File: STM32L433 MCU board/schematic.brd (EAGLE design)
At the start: 55 x 60 mm, 15 parts, among them T1 2N2222, U1 STM32L433CCT6, Y1 ECS-160-8-30B-CKM

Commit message: Add files via upload
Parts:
- removed R1: 1k, SparkFun-Resistors:0603
- removed R2: 220, SparkFun-Resistors:0603
- removed R3: 44.2k, SparkFun-Resistors:0603
- removed R4: 16k, SparkFun-Resistors:0603
- removed R5, R6: 10k, SparkFun-Resistors:0603
- removed Y1: ECS-160-8-30B-CKM, ECS-160-8-30B-CKM:XTAL_ECS-160-8-30B-CKM
- added R10: 1k, adafruit:R0805
- added R11, R12: 10k, adafruit:R0805
- added R7: 44.2k, adafruit:R0805
- added R8: 16k, adafruit:R0805
- added R9: 220, adafruit:R0805
- moved LS1 62.0 mm to (34.3, 47.0)
- moved JP4 2.54 mm to (21.6, 26.7)
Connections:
- removed net N$7: Y1.2, Y1.4
- new net SD_CS: U$1.2, U1.40
- net 3.3V: now also R11.1, R12.1; no longer R5.2, R6.2
- net BUZZ: now also R9.1, U1.29; no longer R2.1
- net CS1: now also U1.41
- net CS2: now also U1.42
- net CS3: now also U1.43
- net CS4: now also U1.45
- net CS5: now also U1.46
- net GND: now also R8.1; no longer R4.1
- net IGN_CHK1: now also U1.11, U1.12
- net IGN_CHK2: now also U1.13
- net IGN_CHK3: now also U1.14
- net LIPO: now also R10.2, R7.2; no longer R1.2, R3.2
- net N$2: now also R9.2; no longer R2.2
- net N$3: now also R10.1; no longer R1.1
- net N$4: now also R11.2; no longer R6.1
- net N$5: now also R7.1, R8.2, U1.10; no longer R3.1, R4.2
- net N$6: now also R12.2; no longer R5.1

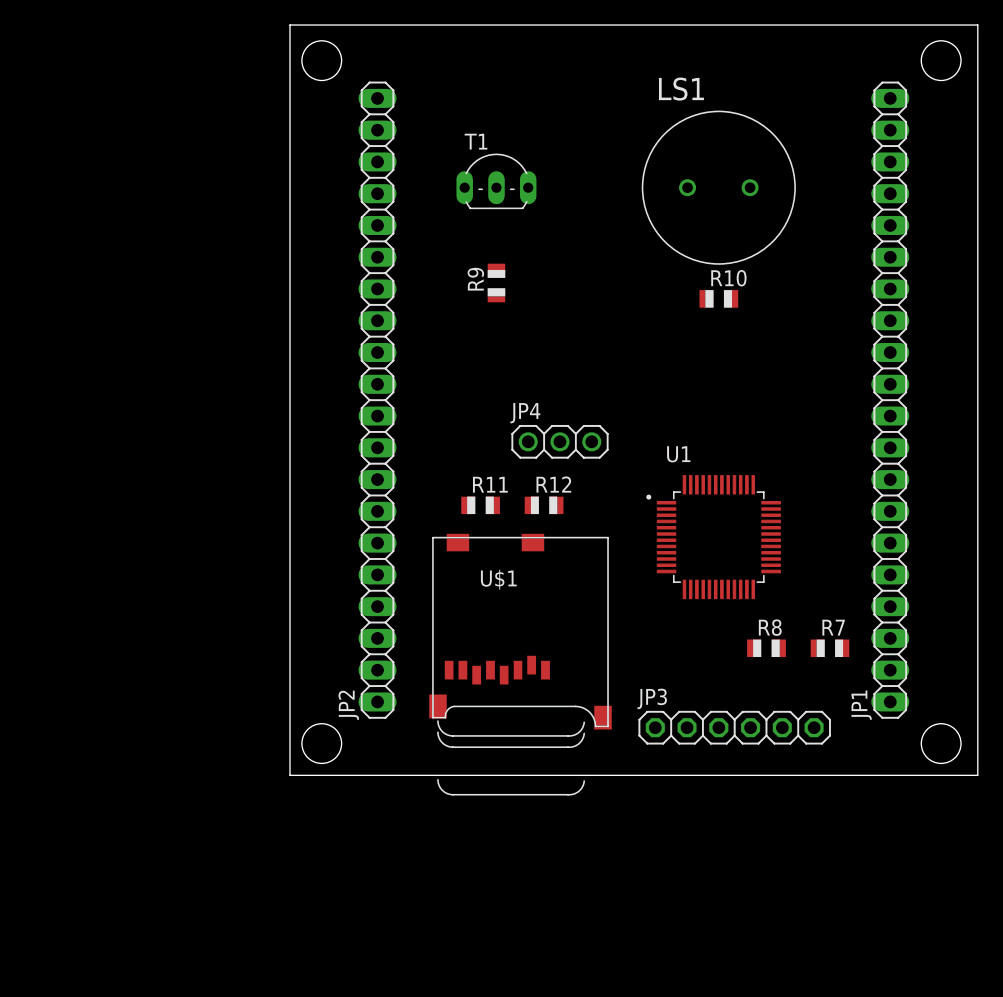
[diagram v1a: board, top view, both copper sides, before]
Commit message: Finished MCU board routing
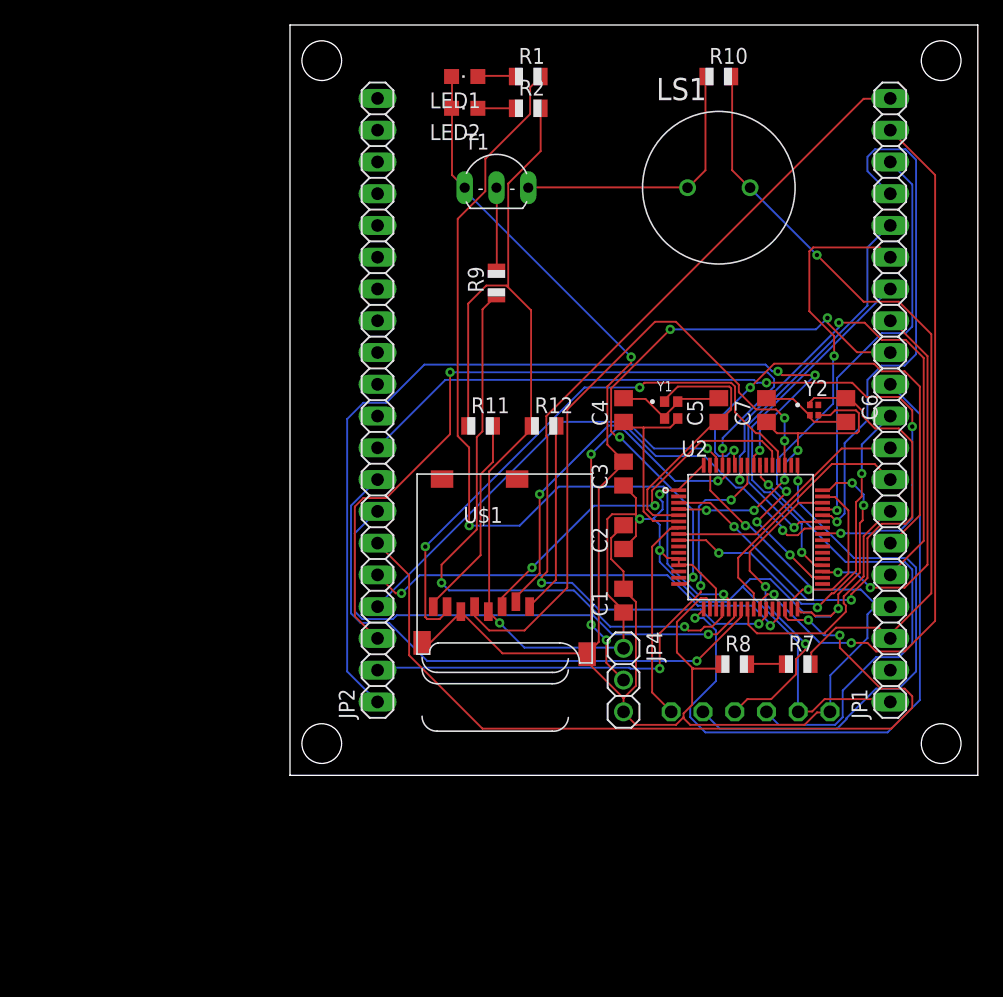
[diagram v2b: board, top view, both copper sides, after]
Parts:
- removed U1: STM32L433CCT6, STM32L433CCT6:QFP50P900X900X160-48N
- added C1: 10nF, rcl:C0805
- added C2: 0.1uF, rcl:C0805
- added C3: 1uF, rcl:C0805
- added C4, C5: 8pF, rcl:C0805
- added C6, C7: 6pF, rcl:C0805
- added LED1: RED, adafruit:CHIPLED_0805
- added LED2: GREEN, adafruit:CHIPLED_0805
- added R1: 130, adafruit:R0805
- added R2: 110, adafruit:R0805
- added U2: STM32L476RCT6, STM32L476RCT6:QFP50P120X120X160-64N
- added Y1: ECS-160-10-37B2-JTN-TR, ECS-160-10-37B2-JTN-TR:XTAL_ECS-160-10-37B2-JTN-TR
- added Y2: ABS04W-32.768KHZ-6-D2-T5, ABS04W-32.768KHZ-6-D2-T5:XTAL_ABS04W-32.768KHZ-6-D2-T5
- moved JP4 19.7 mm to (26.7, 7.62), turned to 270 degrees
- moved R10 17.8 mm to (34.3, 55.9)
- moved R11 6.35 mm to (15.2, 27.9)
- moved R12 6.35 mm to (20.3, 27.9)
- moved U$1 5.24 mm to (10.2, 24.1)
- moved R7 2.84 mm to (40.6, 8.89)
- moved R8 2.84 mm to (35.6, 8.89)
- moved JP3 1.80 mm to (36.8, 5.08), flipped to the bottom
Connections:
- net 5V renamed 3V3.2
- new net ANA_BATT_V: R7.1, R8.2
- new net BOOT: JP4.2, U2.60
- new net N$10: C6.2, C7.2, Y2.2
- new net N$11: C7.1, U2.4, Y2.3
- new net N$12: C6.1, U2.3, Y2.1
- new net N$7: LED1.A, R1.1
- new net N$8: LED2.A, R2.1
- new net N$9: C4.2, C5.2, Y1.2, Y1.4
- new net STAT_LED: R1.2, U2.21
- net 3.3V: now also C1.1, C2.1, C3.1, R2.2, U2.1, U2.12, U2.13, U2.19, U2.32, U2.48, U2.64; no longer U1.1, U1.24, U1.36, U1.48, U1.9
- net BUZZ: now also U2.20; no longer U1.29
- net CS1: now also U2.43; no longer U1.41
- net CS2: now also U2.44; no longer U1.42
- net CS3: now also U2.45; no longer U1.43
- net CS4: now also U2.26; no longer U1.45
- net CS5: now also U2.27; no longer U1.46
- net GND: now also C1.2, C2.2, C3.2, LED1.C, LED2.C, U2.18, U2.31, U2.47, U2.63; no longer U1.23, U1.35, U1.47, U1.8
- net IGN1_1: now also U2.56
- net IGN1_2: now also U2.57
- net IGN2_1: now also U2.61
- net IGN2_2: now also U2.62
- net IGN3_1: now also U2.29
- net IGN3_2: now also U2.30
- net IGN_CHK1: now also U2.22; no longer U1.11, U1.12
- net IGN_CHK2: now also U2.23; no longer U1.13
- net IGN_CHK3: now also U2.41; no longer U1.14
- net MISO: now also U2.35; no longer U1.27
- net MOSI: now also U2.36; no longer U1.28
- net N$1: now also C5.1, U2.5, Y1.1; no longer JP4.2, U1.44
- net N$5: now also C4.1, U2.6, Y1.3; no longer R7.1, R8.2, U1.10
- net NRST: now also U2.7; no longer U1.7
- net RX1: now also U2.24
- net RX2: now also U2.8
- net RX3: now also U2.17
- net SCK: now also U2.34; no longer U1.26
- net SCL0: now also U2.58
- net SDA0: now also U2.59
- net SD_CS: now also U2.42; no longer U1.40
- net SPI1_MISO: now also U2.52; no longer U1.16
- net SPI1_MOSI: now also U2.53; no longer U1.17
- net SPI1_SCK: now also U2.51; no longer U1.15
- net SWCLK: now also U2.49; no longer U1.37
- net SWDIO: now also U2.46; no longer U1.34
- net SWO: now also U2.55; no longer U1.39
- net TX1: now also U2.25
- net TX2: now also U2.9
- net TX3: now also U2.16
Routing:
- net GND: track 0.00 -> 170.2 mm, vias 0 -> 3
- net 3.3V: track 0.00 -> 163.4 mm, vias 0 -> 7
- net IGN1_1: track 0.00 -> 72.4 mm, vias 0 -> 3
- net CS5: track 0.00 -> 71.7 mm, vias 0 -> 2
- net STAT_LED: track 0.00 -> 69.0 mm, vias 0 -> 2
- net IGN3_2: track 0.00 -> 68.3 mm, vias 0 -> 2
- net LIPO: track 0.00 -> 63.2 mm, vias 0 -> 1
- net IGN_CHK3: track 0.00 -> 62.4 mm, vias 0 -> 3
- net IGN2_1: track 0.00 -> 61.0 mm, vias 0 -> 2
- net CS4: track 0.00 -> 58.6 mm, vias 0 -> 2
- net RX3: track 0.00 -> 57.1 mm, vias 0 -> 1
- net SPI1_SCK: track 0.00 -> 51.9 mm, vias 0 -> 2
- net BUZZ: track 0.00 -> 49.9 mm, vias 0 -> 2
- net IGN_CHK2: track 0.00 -> 46.5 mm, vias 0 -> 1
- net SPI1_MISO: track 0.00 -> 46.4 mm, vias 0 -> 2
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
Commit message: Uploaded manufactured PCB design
Doesn't include battery voltage wire :(
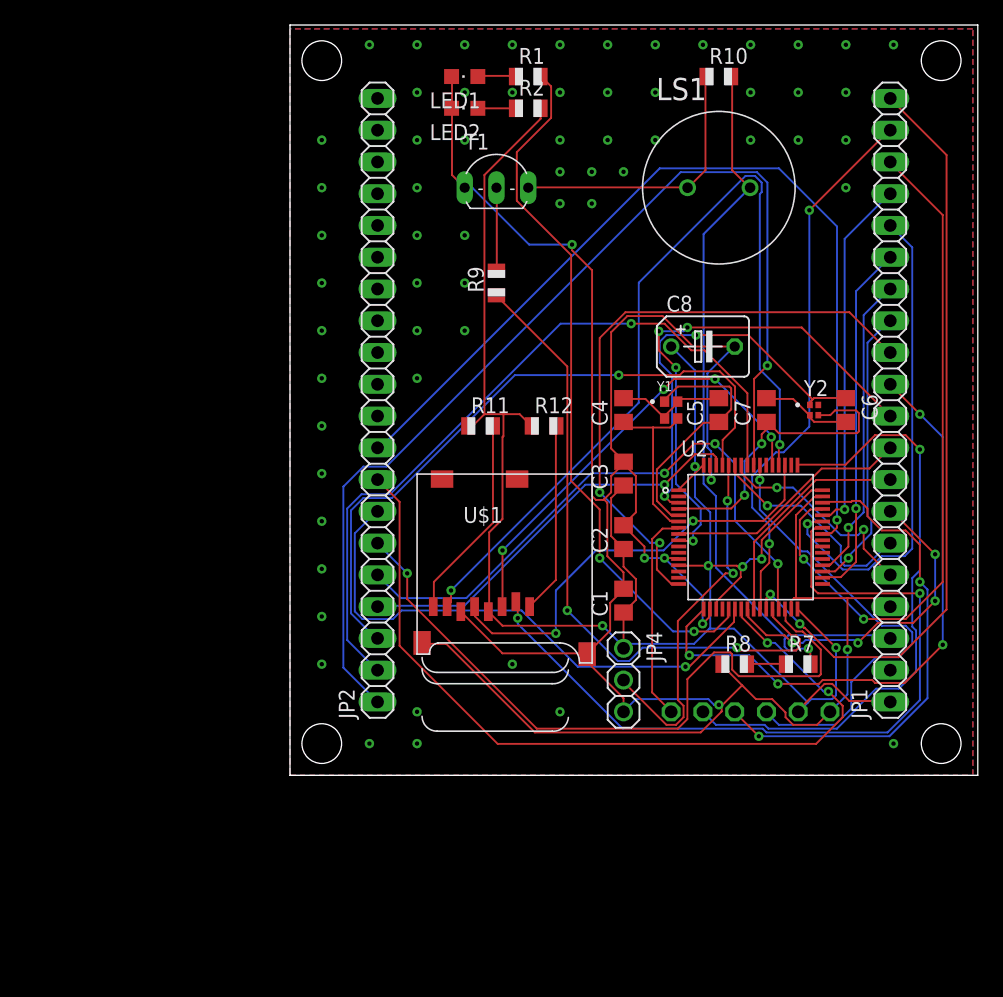
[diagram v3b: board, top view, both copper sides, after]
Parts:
- added C8: 100uF, rcl:B45181B
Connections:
- net 3.3V: now also C8.+; no longer U2.12
- net BUZZ: now also U2.28; no longer U2.20
- net GND: now also C8.-, U2.12
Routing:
- net GND: track 170.2 -> 210.1 mm, vias 3 -> 7
- net SCL0: track 43.5 -> 17.2 mm
- net SD_CS: track 38.3 -> 61.6 mm
- net SPI1_MISO: track 46.4 -> 69.2 mm
- net CS3: track 33.4 -> 55.1 mm, vias 1 -> 2
- net SDA0: track 38.1 -> 17.6 mm, vias 2 -> 1
- net IGN_CHK2: track 46.5 -> 66.2 mm, vias 1 -> 2
- net IGN1_2: track 43.2 -> 60.1 mm, vias 3 -> 1
- net SPI1_SCK: track 51.9 -> 35.3 mm
- net CS4: track 58.6 -> 44.1 mm
- net SWDIO: track 25.5 -> 39.7 mm
- net IGN1_1: track 72.4 -> 86.1 mm, vias 3 -> 1
- net CS2: track 42.2 -> 28.7 mm
- net IGN3_2: track 68.3 -> 55.5 mm, vias 2 -> 1
- net STAT_LED: track 69.0 -> 56.6 mm
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- added copper zone on layer 1, net GND
- added copper zone on layer 16, net GND

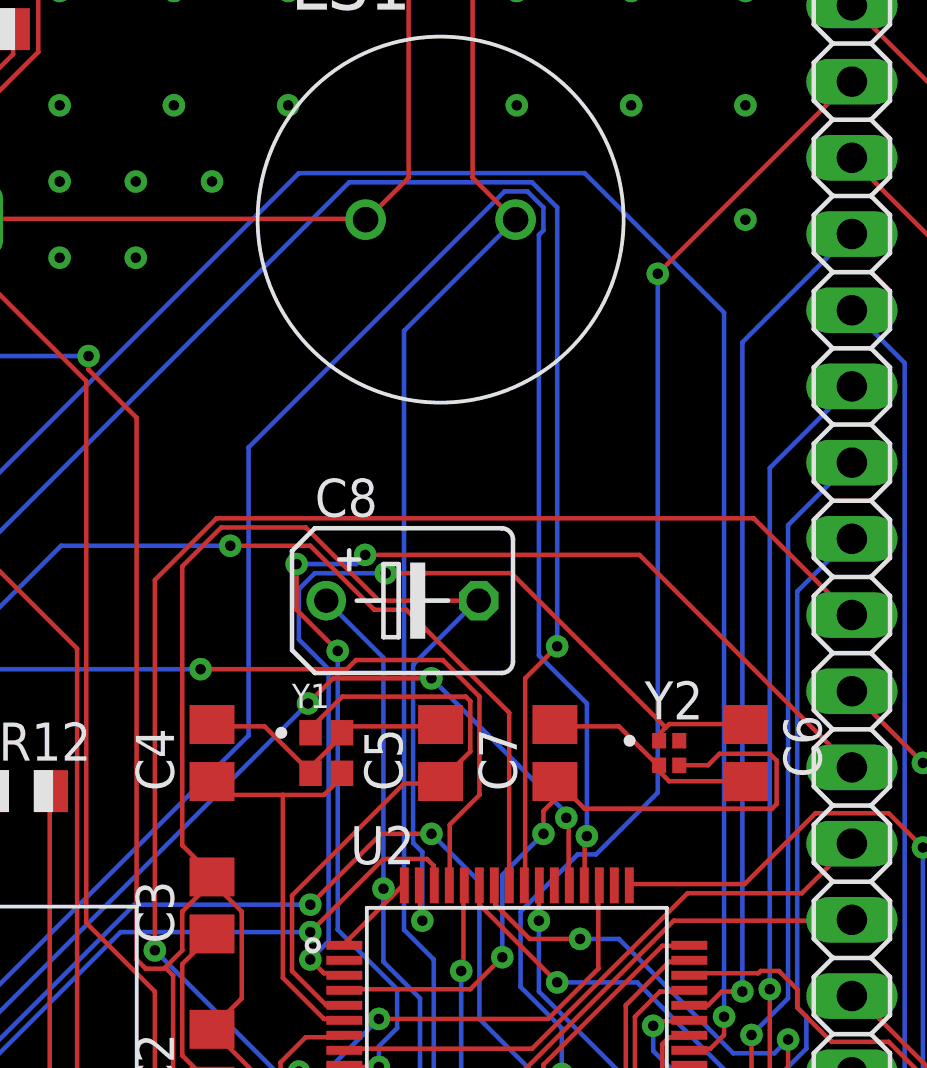
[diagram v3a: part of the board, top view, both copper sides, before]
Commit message: Made some necessary changes for batch 2 :(
That moment when you don't ground the output of oscillators and you don't connect a whole signal lol. At least we get a chance to refine the board
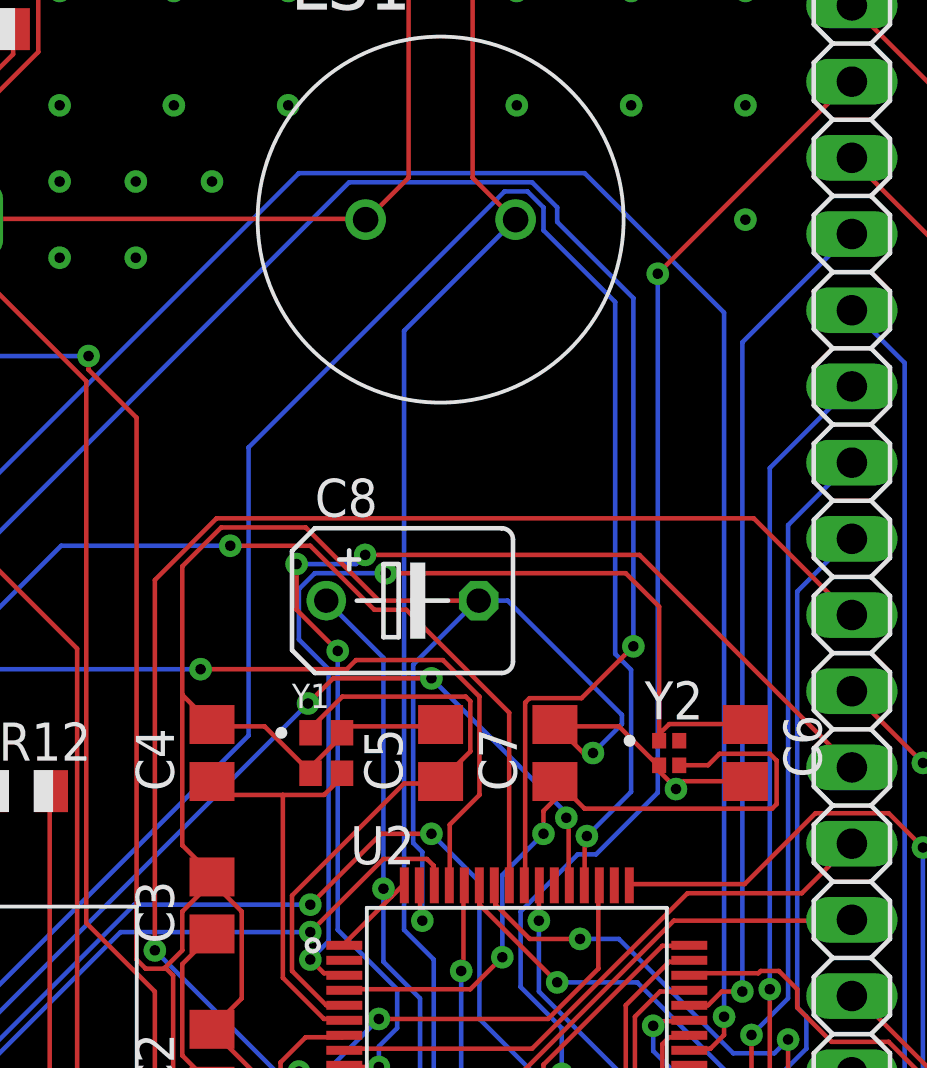
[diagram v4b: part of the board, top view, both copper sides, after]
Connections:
- removed net N$10: C6.2, C7.2, Y2.2
- removed net N$9: C4.2, C5.2, Y1.2, Y1.4
- net ANA_BATT_V: now also U2.10
- net GND: now also C4.2, C5.2, C6.2, C7.2, Y1.2, Y1.4, Y2.2
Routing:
- net GND: track 210.1 -> 238.1 mm, vias 7 -> 9
- net N$9: track 9.29 -> 0.00 mm
- net N$10: track 7.28 -> 0.00 mm
- net IGN1_1: track 86.1 -> 89.2 mm
- net N$12: track 32.2 -> 34.8 mm
- net SPI1_MISO: track 69.2 -> 70.3 mm

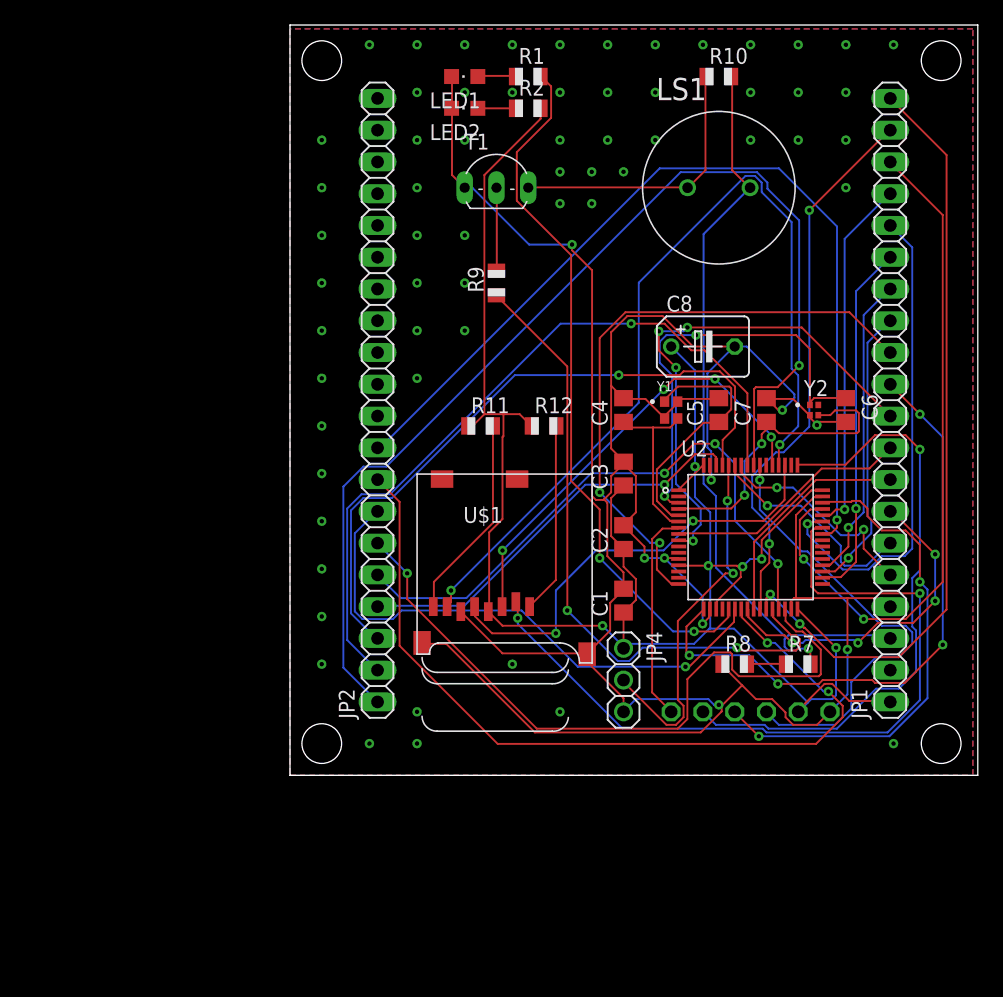
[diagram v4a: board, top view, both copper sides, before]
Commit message: Replaced oscillator components and re-ran autorouter
Still need to route some other wires and check if pinout is good
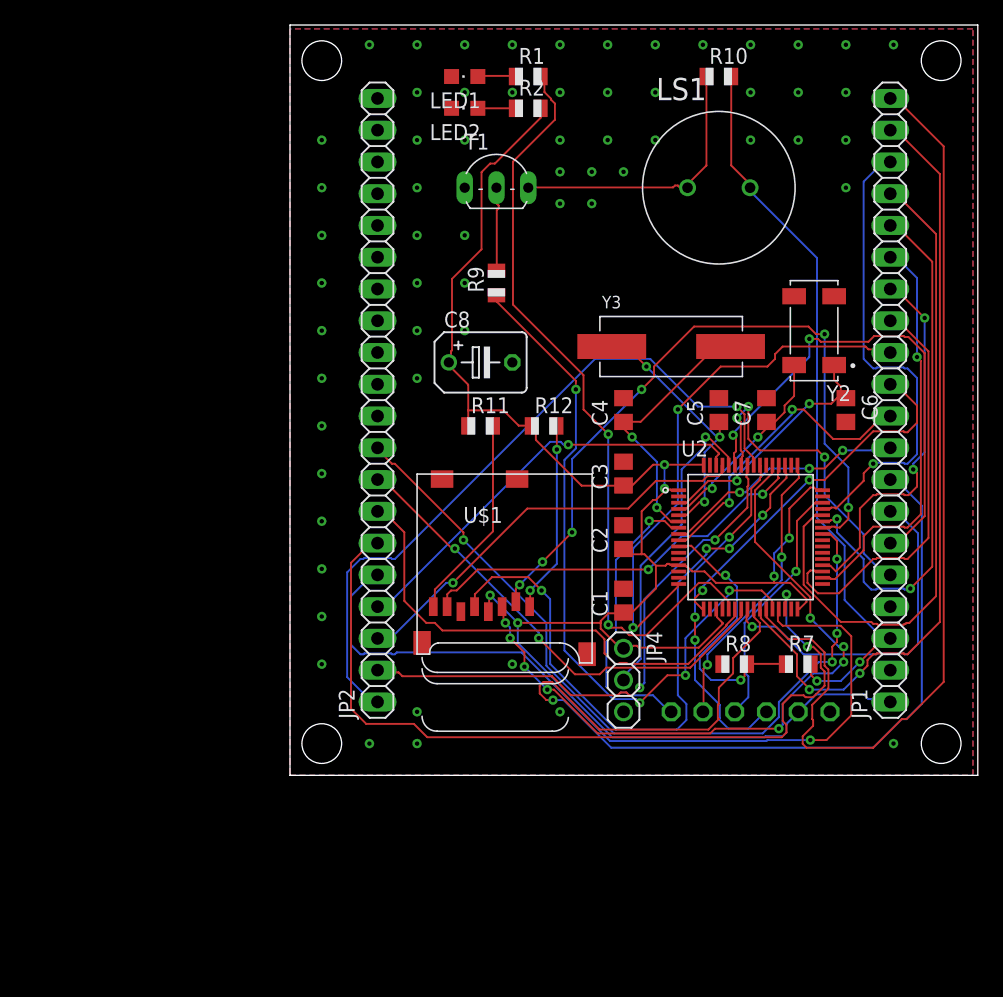
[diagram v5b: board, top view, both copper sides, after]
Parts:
- removed Y1: ECS-160-10-37B2-JTN-TR, ECS-160-10-37B2-JTN-TR:XTAL_ECS-160-10-37B2-JTN-TR
- added Y3: ECS-160-S-5PX-TR, ECS-160-S-5PX-TR:XTAL_ECS-160-S-5PX-TR
- C4, C5: value 8pF -> 7pF
- Y2: value ABS04W-32.768KHZ-6-D2-T5 -> ABS25-32.768KHZ-6-T; device ABS04W-32.768KHZ-6-D2-T5:XTAL_ABS04W-32.768KHZ-6-D2-T5 -> ABS25-32.768KHZ-6-T:XTAL_ABS25-32.768KHZ-6-T
- moved C8 17.8 mm to (15.2, 33.0)
- moved Y2 6.35 mm to (41.9, 35.6), turned to 180 degrees
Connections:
- net GND: no longer Y1.2, Y1.4, Y2.2
- net N$1: now also Y3.1; no longer Y1.1
- net N$11: now also Y2.4; no longer Y2.3
- net N$5: now also Y3.2; no longer Y1.3
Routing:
- net GND: track 238.1 -> 0.00 mm, vias 9 -> 0
- net TX1: track 18.3 -> 80.5 mm, vias 0 -> 1
- net SPI1_MISO: track 70.3 -> 32.5 mm
- net IGN1_1: track 89.2 -> 56.8 mm
- net IGN_CHK2: track 66.2 -> 38.3 mm
- net SWCLK: track 48.9 -> 23.0 mm, vias 1 -> 2
- net CS2: track 28.7 -> 53.4 mm, vias 1 -> 0
- net SDA0: track 17.6 -> 39.6 mm, vias 1 -> 2
- net RX3: track 49.6 -> 29.3 mm, vias 4 -> 2
- net SPI1_MOSI: track 36.0 -> 56.1 mm, vias 4 -> 8
- net IGN2_1: track 53.7 -> 33.7 mm
- net SWDIO: track 39.7 -> 20.3 mm, vias 2 -> 1
- net ANA_BATT_V: track 3.11 -> 22.1 mm, vias 0 -> 2
- net CS4: track 44.1 -> 62.3 mm
- net CS3: track 55.1 -> 37.9 mm, vias 2 -> 1
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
